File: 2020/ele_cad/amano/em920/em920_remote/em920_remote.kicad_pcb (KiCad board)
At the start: 2 copper layers, 40.6 x 58.4 mm, 8 parts, among them SW1 SW_Push, U1 ATtiny85-20PU, U2 TY92SS

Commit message: 緊急停止リモコンのデータ更新
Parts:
- added U3: DCDC_3.3V, em920:DCDC_3.3V, F.Cu at (82.5, 153.0)
- BT1: footprint Connector_PinHeader_2.54mm:PinHeader_1x02_P2.54mm_Vertical -> em920:Battery_UM-4_2; moved to B.Cu
- moved BT1 23.4 mm to (96.5, 157.5), turned to 90 degrees
- moved C1 17.0 mm to (61.0, 154.9)
- moved R1 5.08 mm to (78.7, 139.7)
- moved R2 2.54 mm to (86.4, 127.0)
- moved U2 1.29 mm to (64.8, 107.9)
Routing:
- net +3V3: track 5.08 -> 86.6 mm
- net GND: track 67.3 -> 86.4 mm
- net +BATT: track 0.00 -> 17.8 mm
- net Net-(D1-Pad2): track 5.08 -> 7.62 mm
- net /LED1: track 5.08 -> 7.62 mm
- net /BTN1: track 17.8 -> 20.4 mm
- net /RX: track 50.2 -> 52.7 mm
- net /TX: track 47.2 -> 49.4 mm
- net /RESET: track 52.7 -> 54.0 mm
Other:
- board size 40.6 x 58.4 mm -> 55 x 105 mm

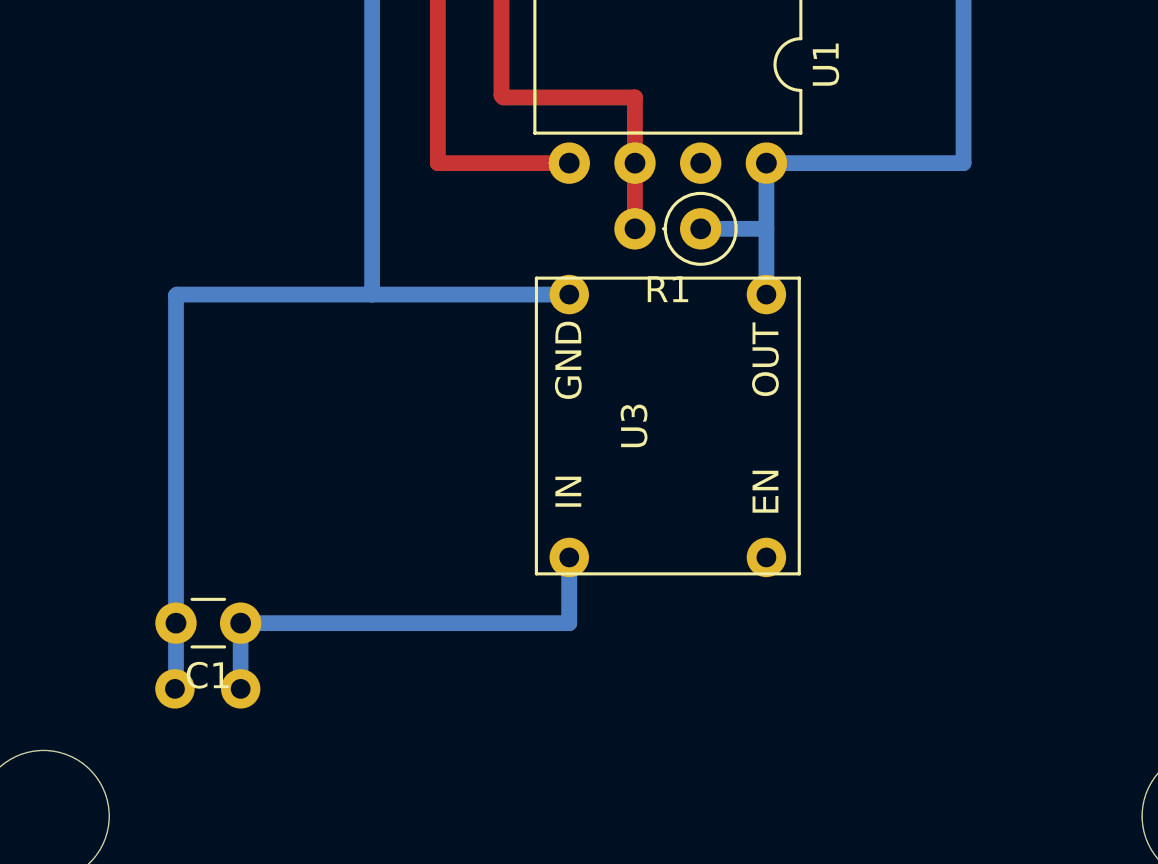
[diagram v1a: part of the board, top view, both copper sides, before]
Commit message: 緊急停止リモコンの更新
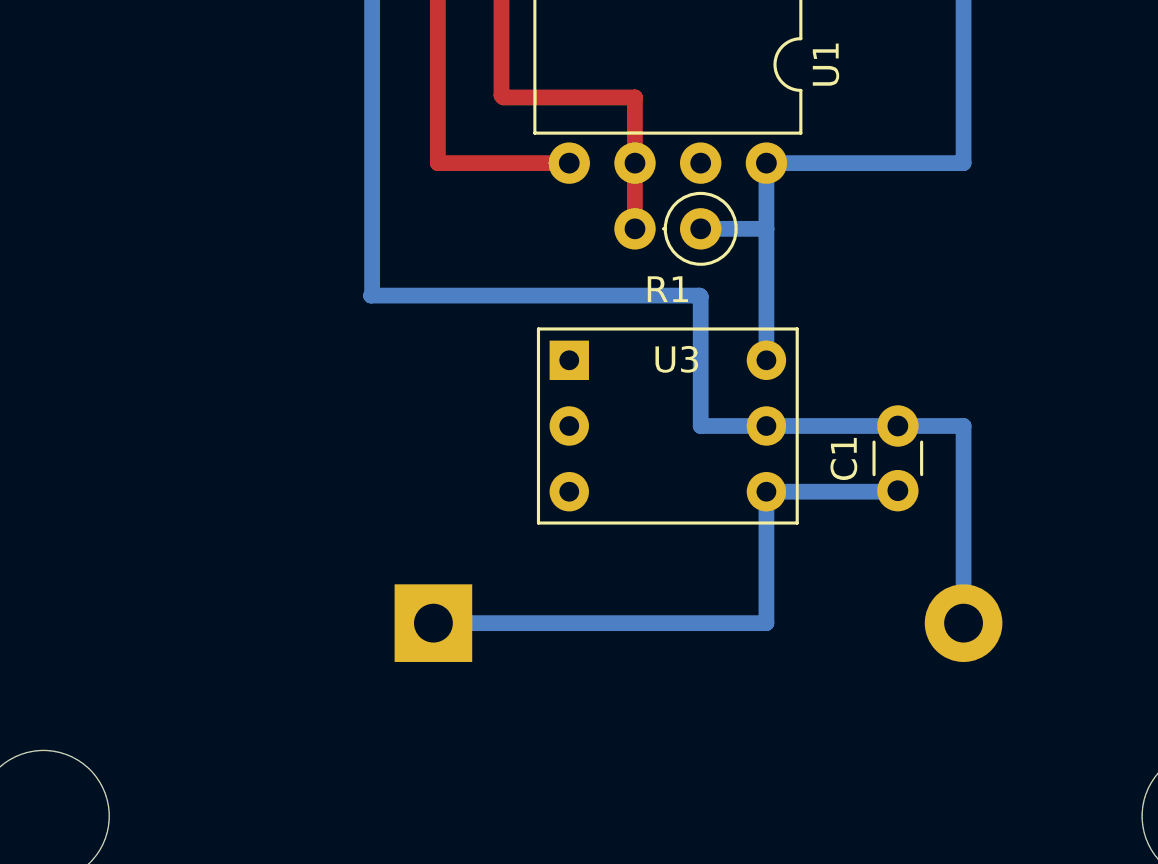
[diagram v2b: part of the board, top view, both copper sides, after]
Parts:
- BT1: footprint em920:Battery_UM-4_2 -> Battery:BatteryHolder_Keystone_103_1x20mm
- U3: value DCDC_3.3V -> AE-XCL102D333CR-G; footprint em920:DCDC_3.3V -> em920:AE-XCL102D333CR-G
- moved BT1 28.2 mm to (68.4, 154.9), turned to 0 degrees
- moved C1 25.9 mm to (86.4, 149.8), turned to 90 degrees
- moved U3 12.1 mm to (73.7, 144.8), turned to 0 degrees
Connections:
- U1 pad 7: (no net) -> Net-(U1-Pad7)
- U2 pad 11: (no net) -> Net-(U2-Pad11)
- U2 pad 12: (no net) -> Net-(U2-Pad12)
- U2 pad 13: (no net) -> Net-(U2-Pad13)
- U2 pad 14: (no net) -> Net-(U2-Pad14)
- U2 pad 15: (no net) -> Net-(U2-Pad15)
- U2 pad 16: (no net) -> Net-(U2-Pad16)
- U2 pad 17: (no net) -> Net-(U2-Pad17)
- U2 pad 18: (no net) -> Net-(U2-Pad18)
- U2 pad 19: (no net) -> Net-(U2-Pad19)
- U2 pad 20: (no net) -> Net-(U2-Pad20)
- U2 pad 4: (no net) -> Net-(U2-Pad4)
- U2 pad 6: (no net) -> Net-(U2-Pad6)
- U2 pad 7: (no net) -> Net-(U2-Pad7)
- U2 pad 8: (no net) -> Net-(U2-Pad8)
- U2 pad 9: (no net) -> Net-(U2-Pad9)
- U3 pad 1: +BATT -> Net-(U3-Pad1)
- U3 pad 2: GND -> Net-(U3-Pad2)
- U3 pad 3: +3V3 -> Net-(U3-Pad3)
- U3 pad 4: (no net) -> +BATT
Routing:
- net GND: track 86.4 -> 91.5 mm
- net +BATT: track 17.8 -> 22.9 mm
- net +3V3: track 86.6 -> 89.1 mm

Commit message: 回路データの更新
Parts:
- added R3: R, Resistor_THT:R_Axial_DIN0207_L6.3mm_D2.5mm_P2.54mm_Vertical, F.Cu at (61.0, 149.9)
- added SW2: SW_SPST, em920:SlideSW, F.Cu at (48.3, 144.8)
- moved R1 1.27 mm to (78.7, 141.0)
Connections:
- U3 pad 1: Net-(U3-Pad1) -> +BATT
- U3 pad 2: Net-(U3-Pad2) -> /PWR_SW
- U3 pad 3: Net-(U3-Pad3) -> GND
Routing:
- net +BATT: track 22.9 -> 48.1 mm
- net GND: track 91.5 -> 115.5 mm
- net /PWR_SW: track 0.00 -> 22.9 mm
- net /BTN1: track 20.4 -> 21.6 mm

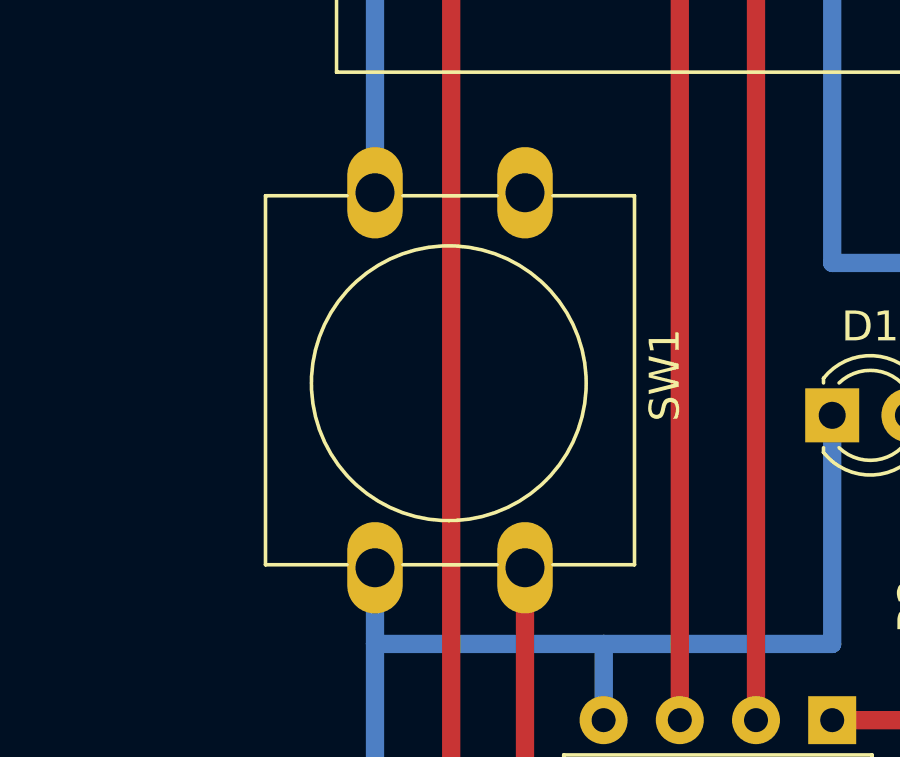
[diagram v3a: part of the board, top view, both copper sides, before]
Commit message: 緊急停止リモコンの回路更新
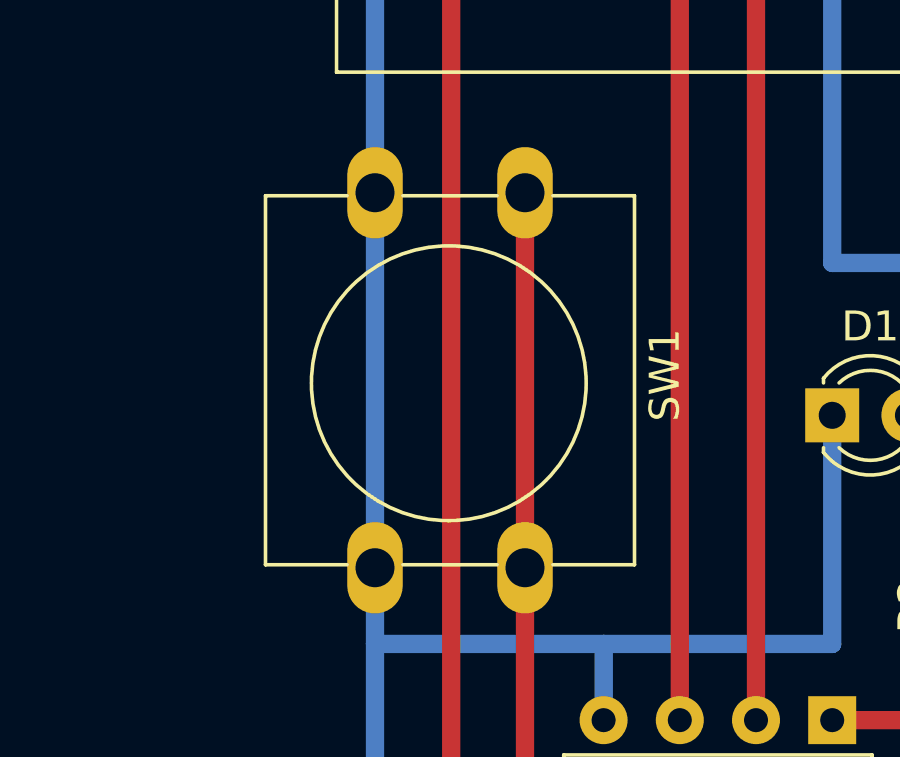
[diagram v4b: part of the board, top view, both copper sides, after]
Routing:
- net GND: track 115.5 -> 128.2 mm
- net /BTN1: track 21.6 -> 34.2 mm

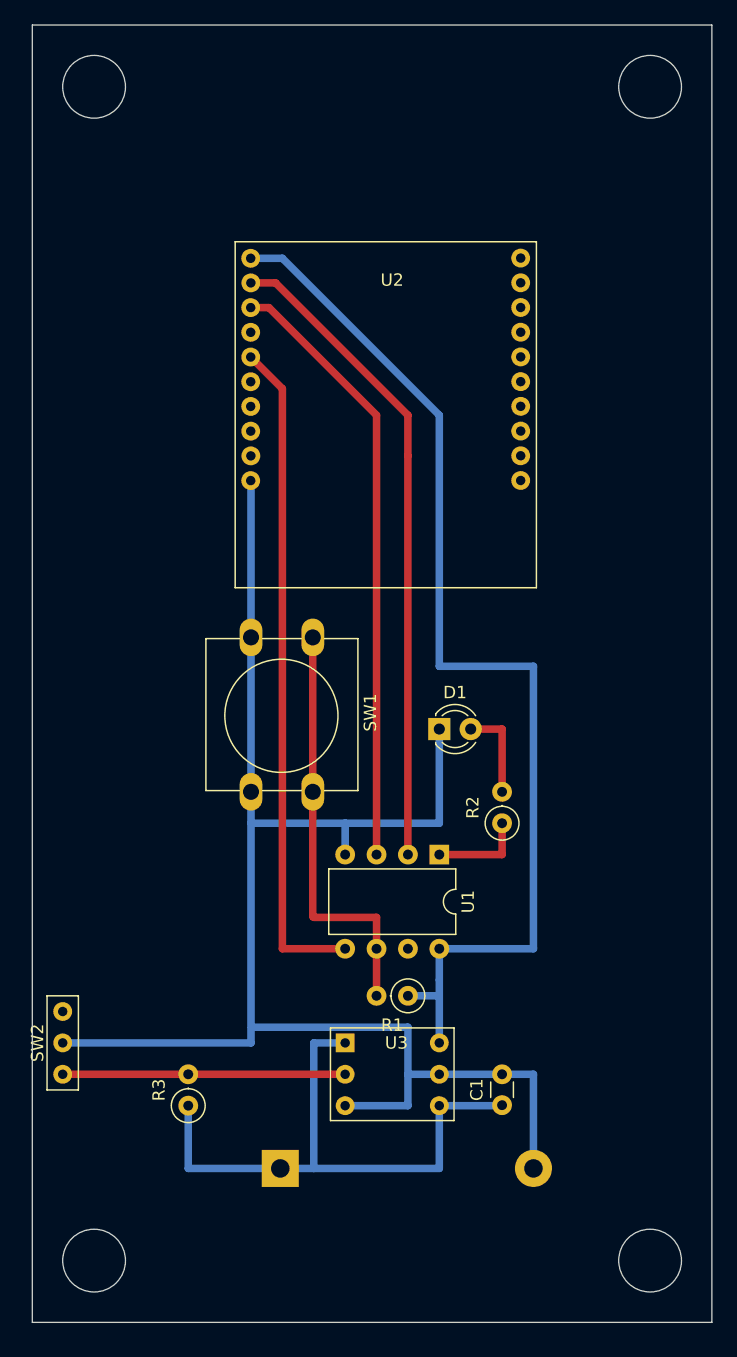
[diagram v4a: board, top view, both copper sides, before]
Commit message: リモコンのDCDCを昇降圧に変更
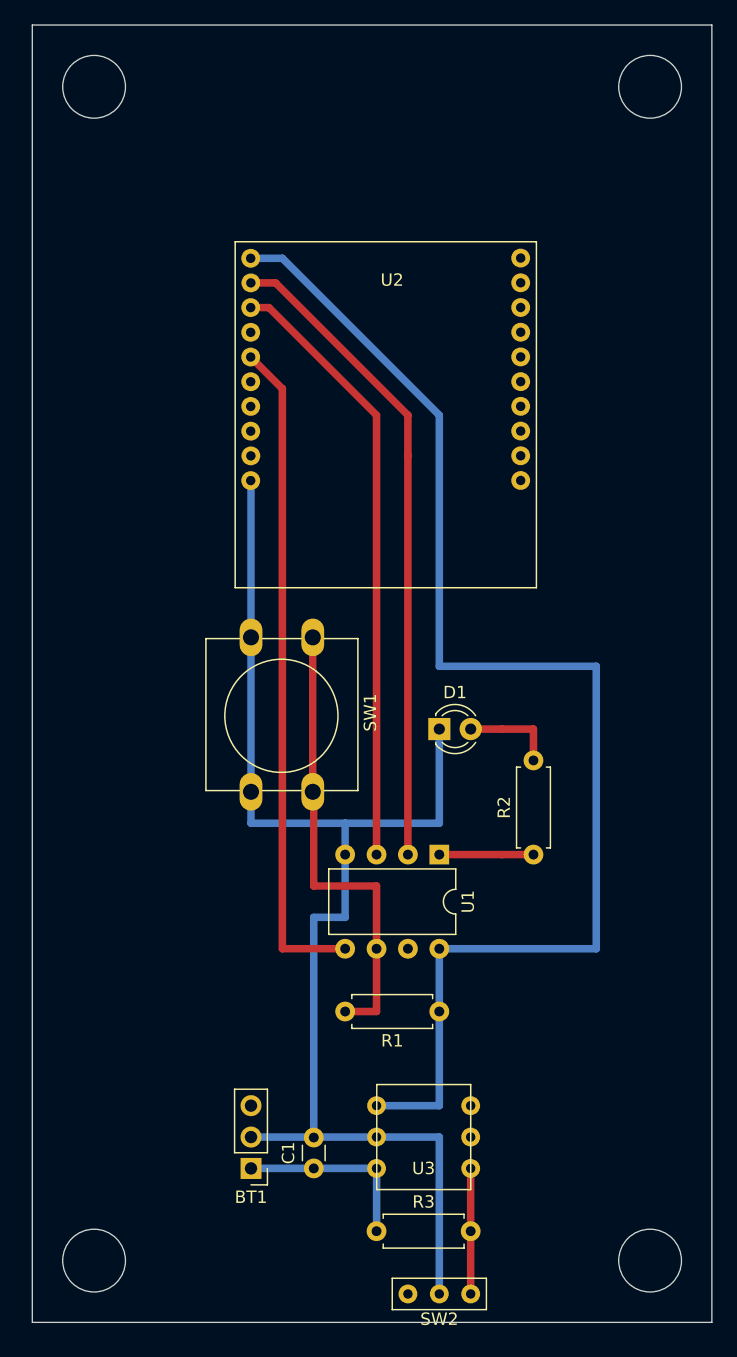
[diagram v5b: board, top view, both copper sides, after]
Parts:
- BT1: footprint Battery:BatteryHolder_Keystone_103_1x20mm -> Connector_PinHeader_2.54mm:PinHeader_1x03_P2.54mm_Vertical; moved to F.Cu
- R1, R2, R3: footprint Resistor_THT:R_Axial_DIN0207_L6.3mm_D2.5mm_P2.54mm_Vertical -> Resistor_THT:R_Axial_DIN0207_L6.3mm_D2.5mm_P7.62mm_Horizontal
- U3: value AE-XCL102D333CR-G -> AE-XC9306-3V3; footprint em920:AE-XCL102D333CR-G -> em920:AE-XC9306-3V3
- moved SW2 40.2 mm to (81.3, 167.6), turned to 180 degrees
- moved R3 18.3 mm to (76.2, 160.0), turned to 0 degrees
- moved C1 16.1 mm to (71.1, 154.9)
- moved U3 14.4 mm to (83.8, 154.9), turned to 180 degrees
- moved R2 3.59 mm to (88.9, 129.5)
- moved R1 2.84 mm to (81.3, 142.2)
- moved BT1 2.37 mm to (66.0, 154.9), turned to 180 degrees
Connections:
- U2 pad 11: Net-(U2-Pad11) -> (no net)
- U2 pad 14: Net-(U2-Pad14) -> (no net)
- U2 pad 15: Net-(U2-Pad15) -> (no net)
- U2 pad 17: Net-(U2-Pad17) -> (no net)
- U2 pad 18: Net-(U2-Pad18) -> (no net)
- U2 pad 19: Net-(U2-Pad19) -> (no net)
- U2 pad 20: Net-(U2-Pad20) -> (no net)
- U2 pad 4: Net-(U2-Pad4) -> (no net)
- U2 pad 6: Net-(U2-Pad6) -> (no net)
- U2 pad 7: Net-(U2-Pad7) -> (no net)
- U2 pad 8: Net-(U2-Pad8) -> (no net)
- U3 pad 2: /PWR_SW -> GND
- U3 pad 3: GND -> +3V3
- U3 pad 4: +BATT -> Net-(U3-Pad4)
- U3 pad 5: GND -> Net-(U3-Pad5)
- U3 pad 6: +3V3 -> /PWR_SW
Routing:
- net +BATT: track 48.1 -> 15.2 mm
- net GND: track 128.2 -> 106.7 mm
- net +3V3: track 89.1 -> 106.9 mm
- net /PWR_SW: track 22.9 -> 10.2 mm
- net /BTN1: track 34.2 -> 38.0 mm

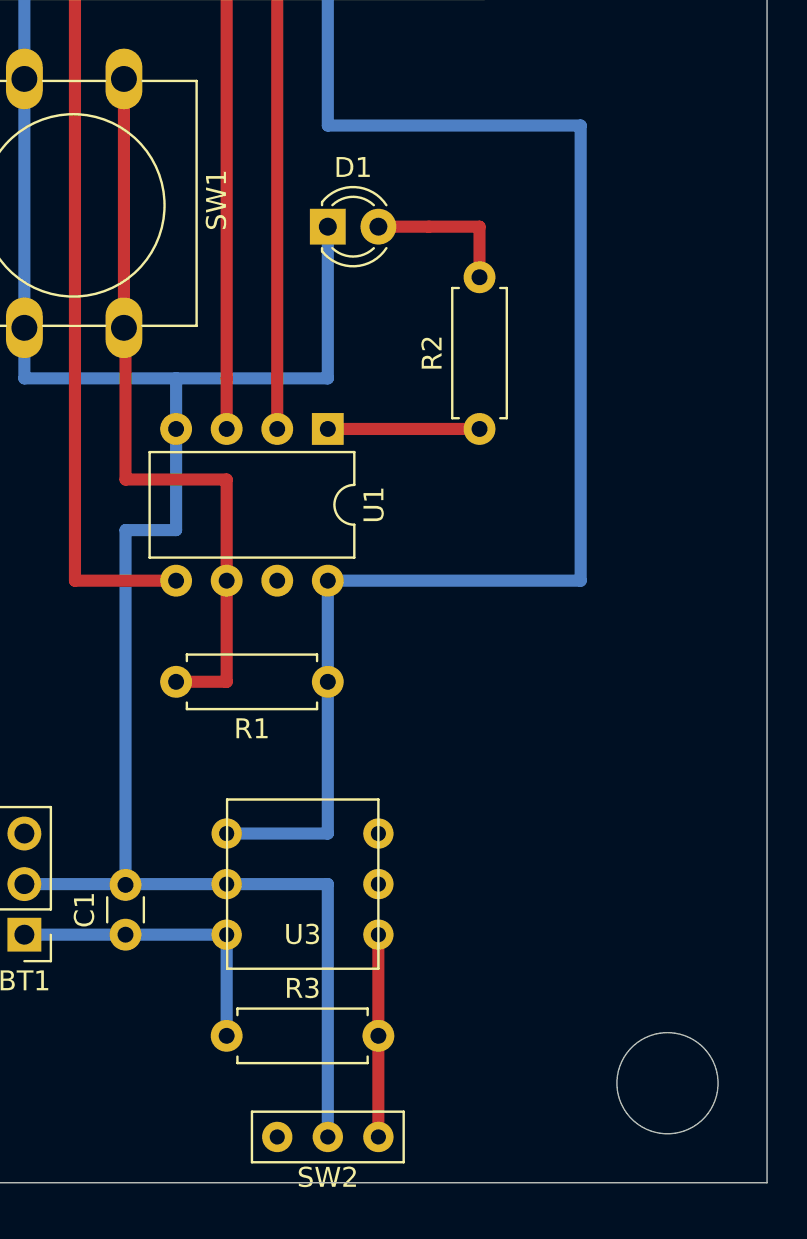
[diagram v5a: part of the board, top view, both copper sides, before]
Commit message: 緊急停止リモコンの更新
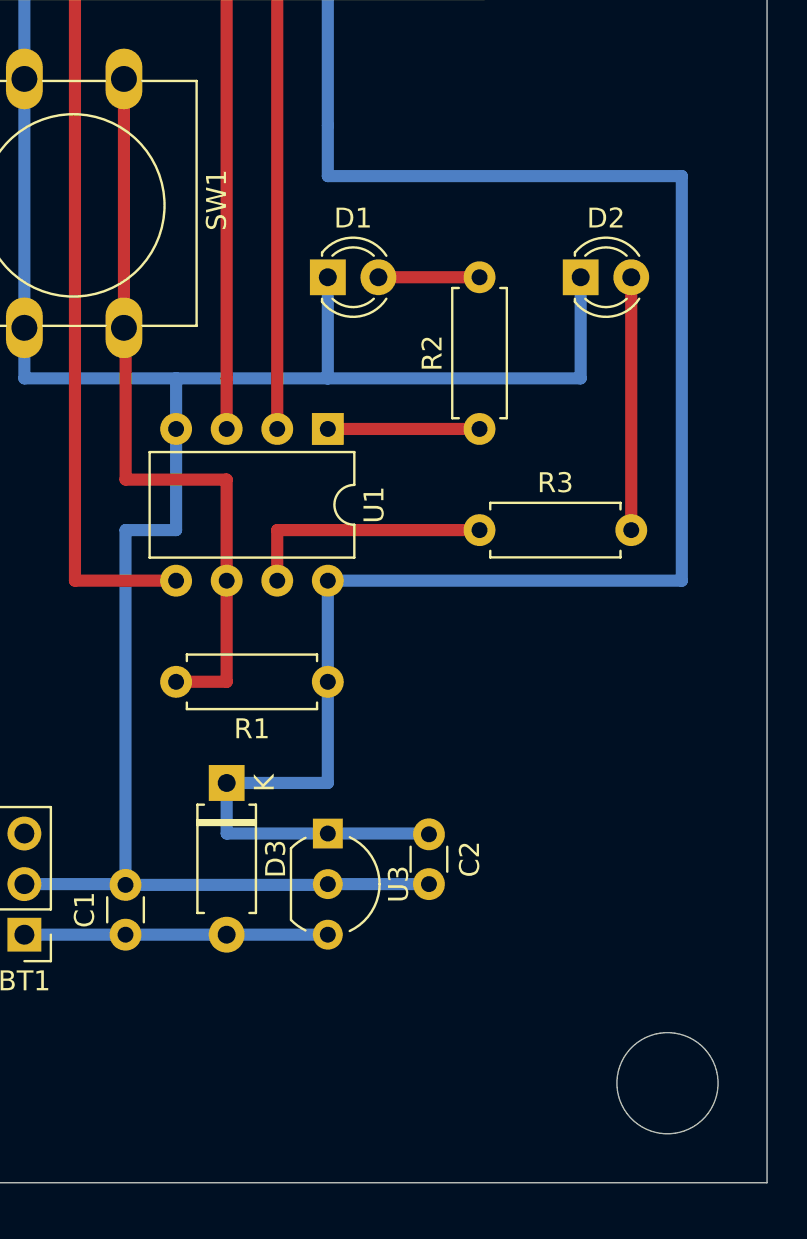
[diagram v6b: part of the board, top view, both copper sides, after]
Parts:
- removed SW2: SW_SPST, em920:SlideSW
- added C2: 2.2uF, Capacitor_THT:C_Disc_D3.0mm_W1.6mm_P2.50mm, F.Cu at (86.4, 149.9)
- added D2: LED, LED_THT:LED_D3.0mm_FlatTop, F.Cu at (94.0, 121.9)
- added D3: DIODE, Diode_THT:D_A-405_P7.62mm_Horizontal, F.Cu at (76.2, 147.3)
- C1: value 0.1uF -> 0.33uF
- U3: value AE-XC9306-3V3 -> LP2950-3.3_TO92; footprint em920:AE-XC9306-3V3 -> Package_TO_SOT_THT:TO-92_Inline_Wide
- moved R3 28.4 mm to (88.9, 134.6)
- moved U3 5.68 mm to (81.3, 149.9), turned to 270 degrees
- moved D1 2.54 mm to (81.3, 121.9)
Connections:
- R3 pad 1: +BATT -> /LED2
- R3 pad 2: /PWR_SW -> Net-(D2-Pad2)
- U1 pad 7: Net-(U1-Pad7) -> /LED2
- U3 pad 1: +BATT -> +3V3
- U3 pad 3: +3V3 -> +BATT
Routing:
- net +3V3: track 106.9 -> 127.2 mm
- net Net-(D2-Pad2): track 0.00 -> 12.7 mm
- net /LED2: track 0.00 -> 12.7 mm
- net /PWR_SW: track 10.2 -> 0.00 mm
- net GND: track 106.7 -> 114.4 mm
- net Net-(D1-Pad2): track 7.62 -> 5.08 mm
